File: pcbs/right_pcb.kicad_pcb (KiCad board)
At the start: 2 copper layers, 161.7 x 89.3 mm, 54 parts

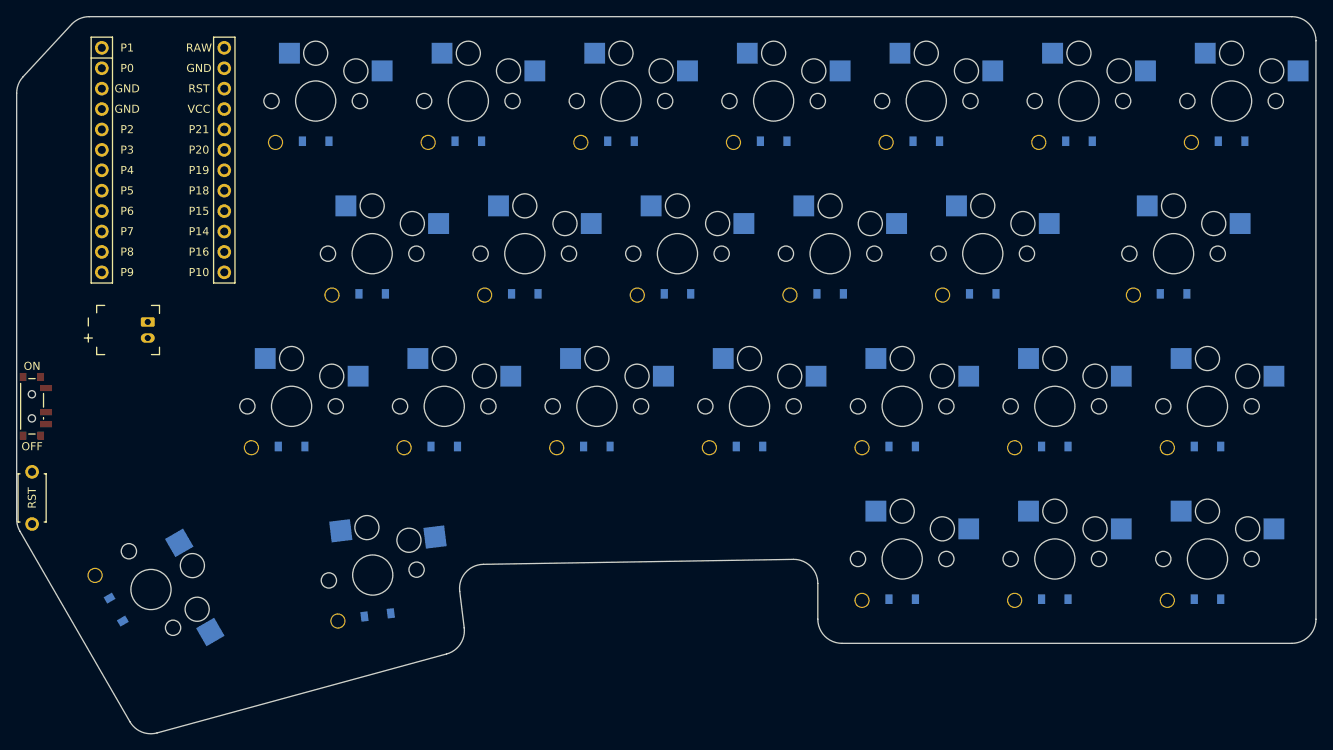
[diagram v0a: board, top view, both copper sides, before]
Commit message: right side mx switches and row and column nets
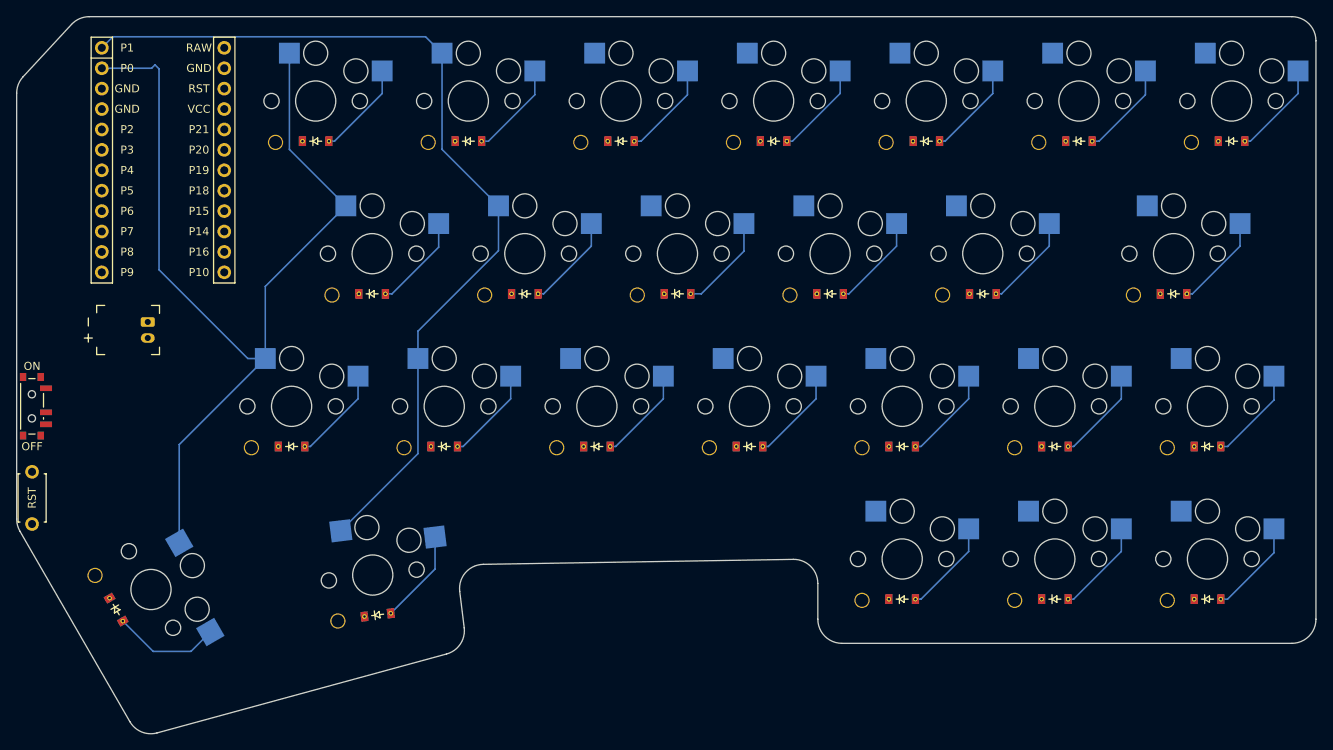
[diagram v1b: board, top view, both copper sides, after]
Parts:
- D1, D10, D11, D12, D13, D14, D15, D16, D17, D18, D19, D2, D20, D21, D22, D23, D24, D25, D3, D4, D5, D6, D7, D8, D9: footprint ceoloide:diode_tht_sod123 -> ComboDiode; moved to F.Cu
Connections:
- D1 pad 1: (no net) -> y_single
- D10 pad 1: (no net) -> k_single
- D11 pad 1: (no net) -> l_single
- D12 pad 1: (no net) -> colon_single
- D13 pad 1: (no net) -> quotes_single
- D14 pad 1: (no net) -> b_single
- D15 pad 1: (no net) -> n_single
- D16 pad 1: (no net) -> m_single
- D17 pad 1: (no net) -> comma_single
- D18 pad 1: (no net) -> peroid_single
- D19 pad 1: (no net) -> up_arrow_single
- D2 pad 1: (no net) -> u_single
- D20 pad 1: (no net) -> slash_single
- D21 pad 1: (no net) -> larrow_single
- D22 pad 1: (no net) -> darrow_single
- D23 pad 1: (no net) -> rarrow_single
- D24 pad 1: (no net) -> space_single
- D25 pad 1: (no net) -> raise_single
- D3 pad 1: (no net) -> i_single
- D4 pad 1: (no net) -> o_single
- D5 pad 1: (no net) -> p_single
- D6 pad 1: (no net) -> backspace_single
- D7 pad 1: (no net) -> delete_single
- D8 pad 1: (no net) -> h_single
- D9 pad 1: (no net) -> j_single
- S1 pad 1: (no net) -> P0
- S10 pad 1: (no net) -> P2
- S11 pad 1: (no net) -> P3
- S12 pad 1: (no net) -> P4
- S13 pad 1: (no net) -> P5
- S14 pad 1: (no net) -> P0
- S15 pad 1: (no net) -> P1
- S16 pad 1: (no net) -> P2
- S17 pad 1: (no net) -> P3
- S18 pad 1: (no net) -> P4
- S19 pad 1: (no net) -> P5
- S2 pad 1: (no net) -> P1
- S20 pad 1: (no net) -> P6
- S21 pad 1: (no net) -> P4
- S22 pad 1: (no net) -> P5
- S23 pad 1: (no net) -> P6
- S24 pad 1: (no net) -> P0
- S25 pad 1: (no net) -> P1
- S3 pad 1: (no net) -> P2
- S4 pad 1: (no net) -> P3
- S5 pad 1: (no net) -> P4
- S6 pad 1: (no net) -> P5
- S7 pad 1: (no net) -> P6
- S8 pad 1: (no net) -> P0
- S9 pad 1: (no net) -> P1
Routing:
- net P0: track 0.00 -> 122.7 mm
- net P1: track 0.00 -> 114.3 mm
- net space_single: track 0.00 -> 13.4 mm
- net k_single: track 0.00 -> 12.3 mm
- net slash_single: track 0.00 -> 12.0 mm
- net rarrow_single: track 0.00 -> 12.0 mm
- net u_single: track 0.00 -> 12.0 mm
- net i_single: track 0.00 -> 12.0 mm
- net backspace_single: track 0.00 -> 12.0 mm
- net h_single: track 0.00 -> 12.0 mm
- net delete_single: track 0.00 -> 11.9 mm
- net y_single: track 0.00 -> 11.9 mm
- net quotes_single: track 0.00 -> 11.9 mm
- net p_single: track 0.00 -> 11.9 mm
- net o_single: track 0.00 -> 11.9 mm
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
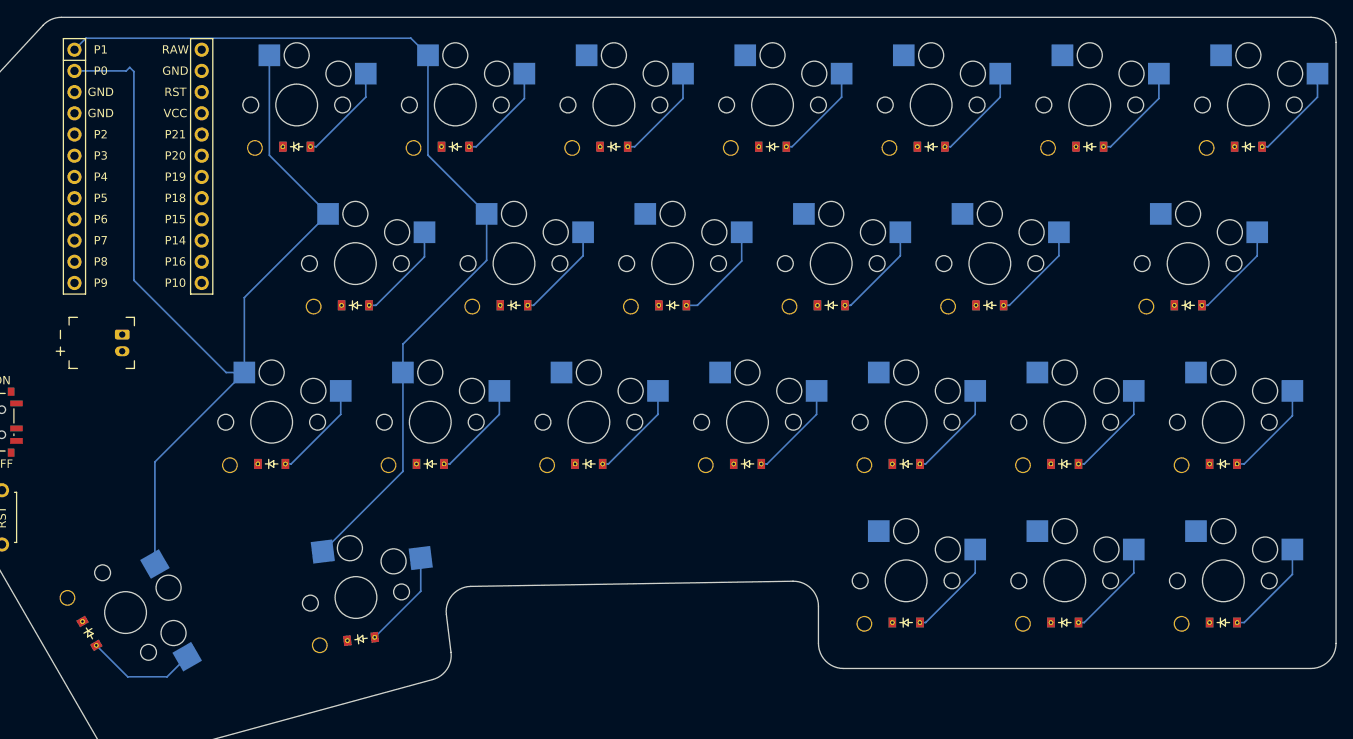
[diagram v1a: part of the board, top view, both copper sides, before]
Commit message: right side changes like mx switch
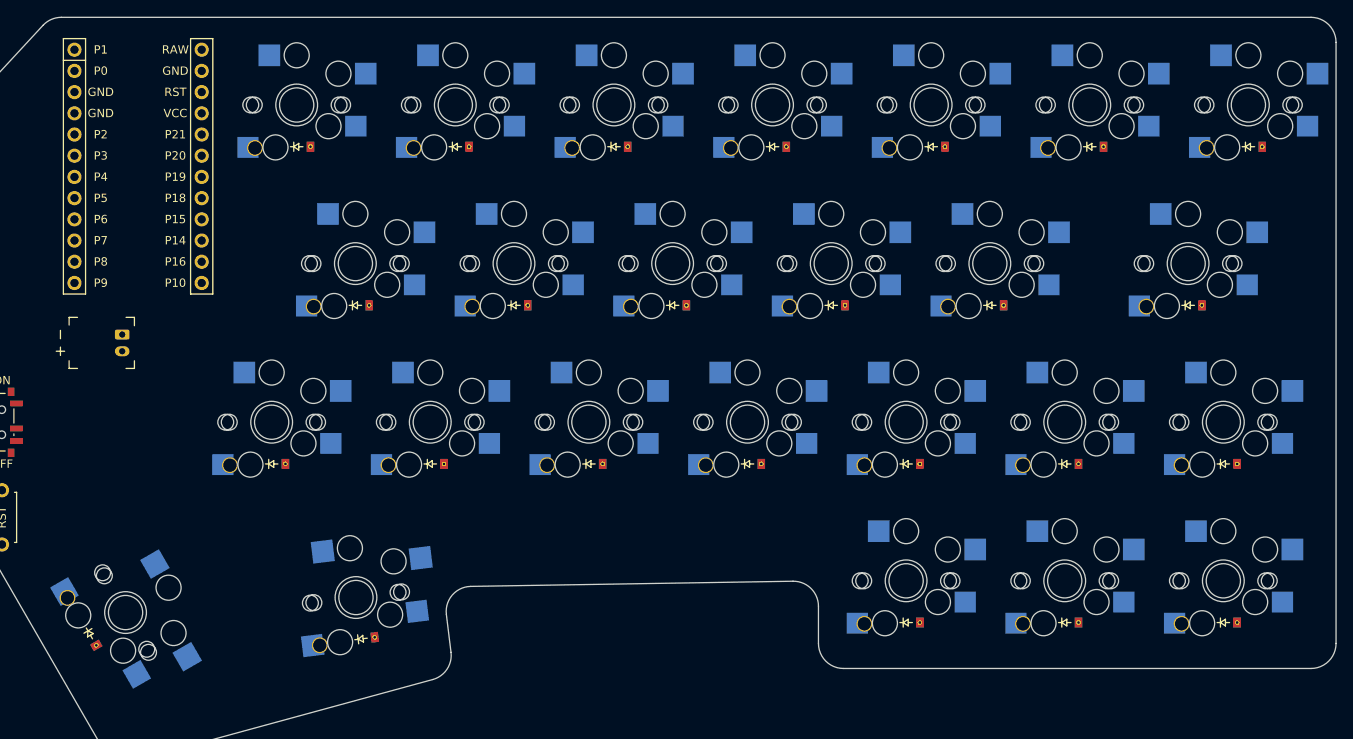
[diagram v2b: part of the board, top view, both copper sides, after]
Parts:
- added S26: , ceoloide:switch_mx, B.Cu at (150.0, 100.0)
- added S27: , ceoloide:switch_mx, B.Cu at (169.0, 100.0)
- added S28: , ceoloide:switch_mx, B.Cu at (188.0, 100.0)
- added S29: , ceoloide:switch_mx, B.Cu at (207.0, 100.0)
- added S30: , ceoloide:switch_mx, B.Cu at (226.0, 100.0)
- added S31: , ceoloide:switch_mx, B.Cu at (245.0, 100.0)
- added S32: , ceoloide:switch_mx, B.Cu at (264.0, 100.0)
- added S33: , ceoloide:switch_mx, B.Cu at (157.0, 119.0)
- added S34: , ceoloide:switch_mx, B.Cu at (176.0, 119.0)
- added S35: , ceoloide:switch_mx, B.Cu at (195.0, 119.0)
- added S36: , ceoloide:switch_mx, B.Cu at (214.0, 119.0)
- added S37: , ceoloide:switch_mx, B.Cu at (233.0, 119.0)
- added S38: , ceoloide:switch_mx, B.Cu at (256.8, 119.0)
- added S39: , ceoloide:switch_mx, B.Cu at (147.0, 138.0)
- added S40: , ceoloide:switch_mx, B.Cu at (166.0, 138.0)
- added S41: , ceoloide:switch_mx, B.Cu at (185.0, 138.0)
- added S42: , ceoloide:switch_mx, B.Cu at (204.0, 138.0)
- added S43: , ceoloide:switch_mx, B.Cu at (223.0, 138.0)
- added S44: , ceoloide:switch_mx, B.Cu at (242.0, 138.0)
- added S45: , ceoloide:switch_mx, B.Cu at (261.0, 138.0)
- added S46: , ceoloide:switch_mx, B.Cu at (223.0, 157.0)
- added S47: , ceoloide:switch_mx, B.Cu at (242.0, 157.0)
- added S48: , ceoloide:switch_mx, B.Cu at (261.0, 157.0)
- added S49: , ceoloide:switch_mx, B.Cu at (129.5, 160.8)
- added S50: , ceoloide:switch_mx, B.Cu at (157.1, 159.0)
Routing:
- net P0: track 122.7 -> 0.00 mm
- net P1: track 114.3 -> 0.00 mm
- net space_single: track 13.4 -> 0.00 mm
- net k_single: track 12.3 -> 0.00 mm
- net slash_single: track 12.0 -> 0.00 mm
- net rarrow_single: track 12.0 -> 0.00 mm
- net u_single: track 12.0 -> 0.00 mm
- net i_single: track 12.0 -> 0.00 mm
- net backspace_single: track 12.0 -> 0.00 mm
- net h_single: track 12.0 -> 0.00 mm
- net delete_single: track 11.9 -> 0.00 mm
- net y_single: track 11.9 -> 0.00 mm
- net quotes_single: track 11.9 -> 0.00 mm
- net p_single: track 11.9 -> 0.00 mm
- net o_single: track 11.9 -> 0.00 mm
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
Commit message: pcbs finished for now
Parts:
- added G***: LOGO, LOGO, F.Cu at (131.2, 143.5)
- S1, S10, S11, S12, S13, S14, S15, S16, S17, S18, S19, S2, S20, S21, S22, S23, S24, S25, S3, S4, S5, S6, S7, S8, S9: footprint ceoloide:switch_choc_v1_v2 -> anotherchocswitch:switch_choc_v1_v2
- moved D1 3.00 mm to (150.0, 108.0)
- moved D10 3.00 mm to (195.0, 127.0)
- moved D11 3.00 mm to (214.0, 127.0)
- moved D12 3.00 mm to (233.0, 127.0)
- moved D13 3.00 mm to (256.8, 127.0)
- moved D14 3.00 mm to (147.0, 146.0)
- moved D15 3.00 mm to (166.0, 146.0)
- moved D16 3.00 mm to (185.0, 146.0)
- moved D17 3.00 mm to (204.0, 146.0)
- moved D18 3.00 mm to (223.0, 146.0)
- moved D19 3.00 mm to (242.0, 146.0)
- moved D2 3.00 mm to (169.0, 108.0)
- moved D20 3.00 mm to (261.0, 146.0)
- moved D21 3.00 mm to (223.0, 165.0)
- moved D22 3.00 mm to (242.0, 165.0)
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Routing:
- net P5: track 0.00 -> 378.3 mm
- net P4: track 0.00 -> 323.9 mm
- net P6: track 0.00 -> 310.3 mm
- net P1: track 0.00 -> 238.9 mm, vias 0 -> 4
- net P3: track 0.00 -> 234.9 mm
- net P9: track 0.00 -> 225.0 mm
- net P2: track 0.00 -> 213.0 mm
- net P0: track 0.00 -> 207.2 mm, vias 0 -> 2
- net P8: track 0.00 -> 189.1 mm
- net GND: track 0.00 -> 185.3 mm
- net P7: track 0.00 -> 182.3 mm
- net P10: track 0.00 -> 163.3 mm
- net P14: track 0.00 -> 93.2 mm
- net RST: track 0.00 -> 63.8 mm
- net RAW: track 0.00 -> 62.8 mm
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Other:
- board text added: "(symbol "LOGO" (pin_names (offset 1.016)) (in_bom yes) (on_board yes) (property "Reference" "#G" (at 0 1.36563 0) (effects (font (size 1.27 1.27)) hide) ) (property "Value" "LOGO" (at 0 -1.36563 0) (effects (font (size 1.27 1.27)) hide) ) (property "Footprint" "" (at 0 0 0) (effects (font (size 1.27 1.27)) hide) ) (property "Datasheet" "" (at 0 0 0) (effects (font (size 1.27 1.27)) hide) ) (symbo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"
- board text added: "Caeserua"
- board text added: "{dblquote}Caeseura{dblquote} by theb0b, 2/26"
